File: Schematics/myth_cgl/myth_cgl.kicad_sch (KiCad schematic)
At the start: 9 parts, among them U1002 74LS08, U1003 74LS32, U1013 74AHC04, U1019 74HC02, U1020 74AHC138, U1021 74AHC138, U1022 74AHC244

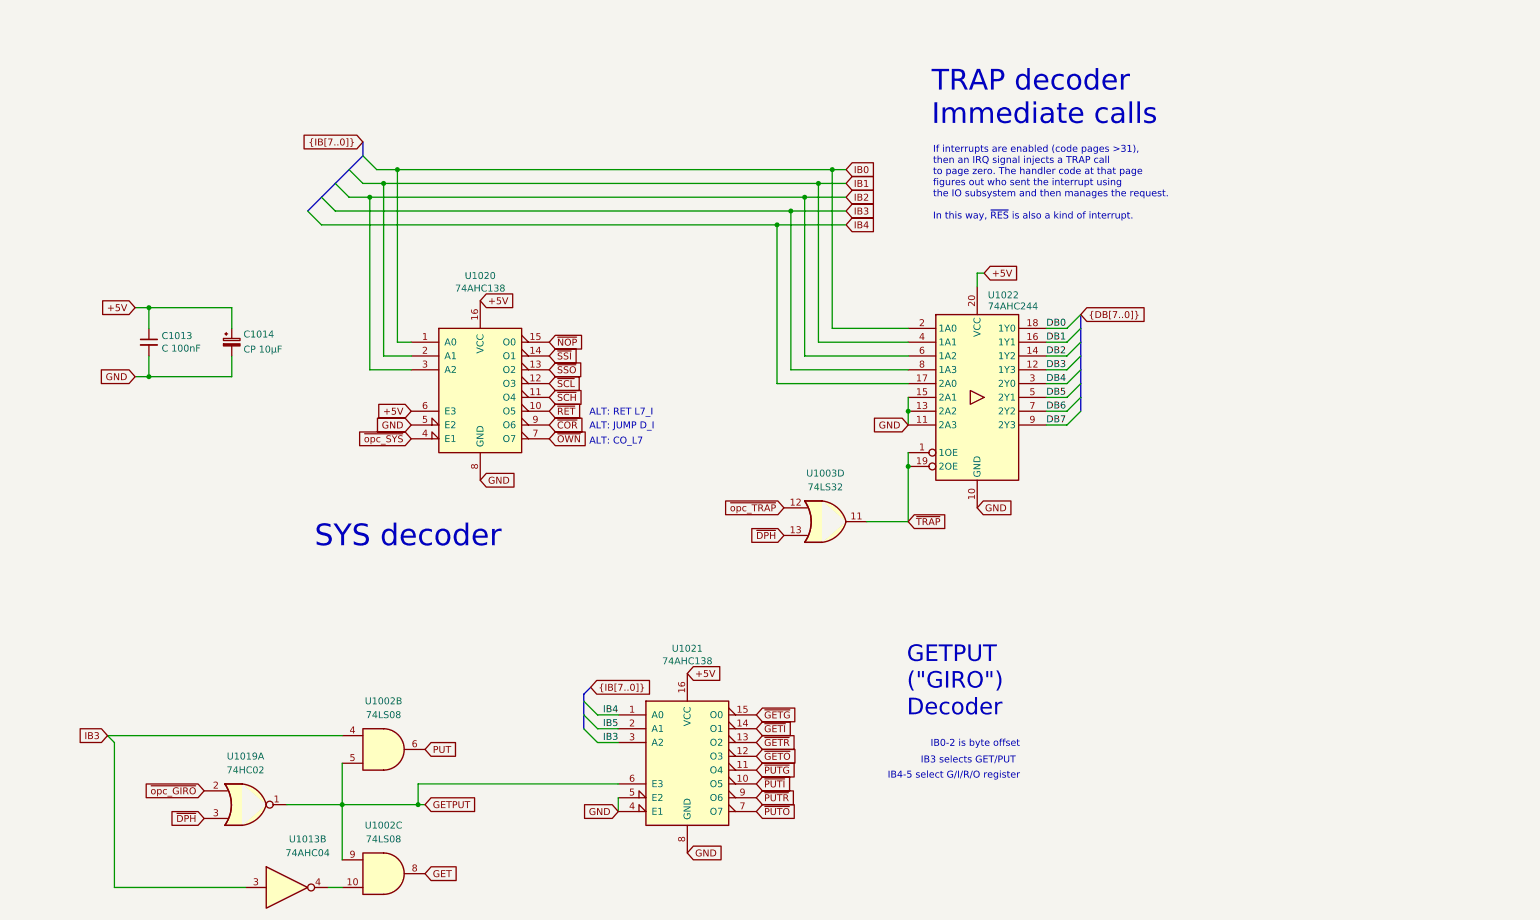
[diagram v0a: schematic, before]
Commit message: Change CO do D
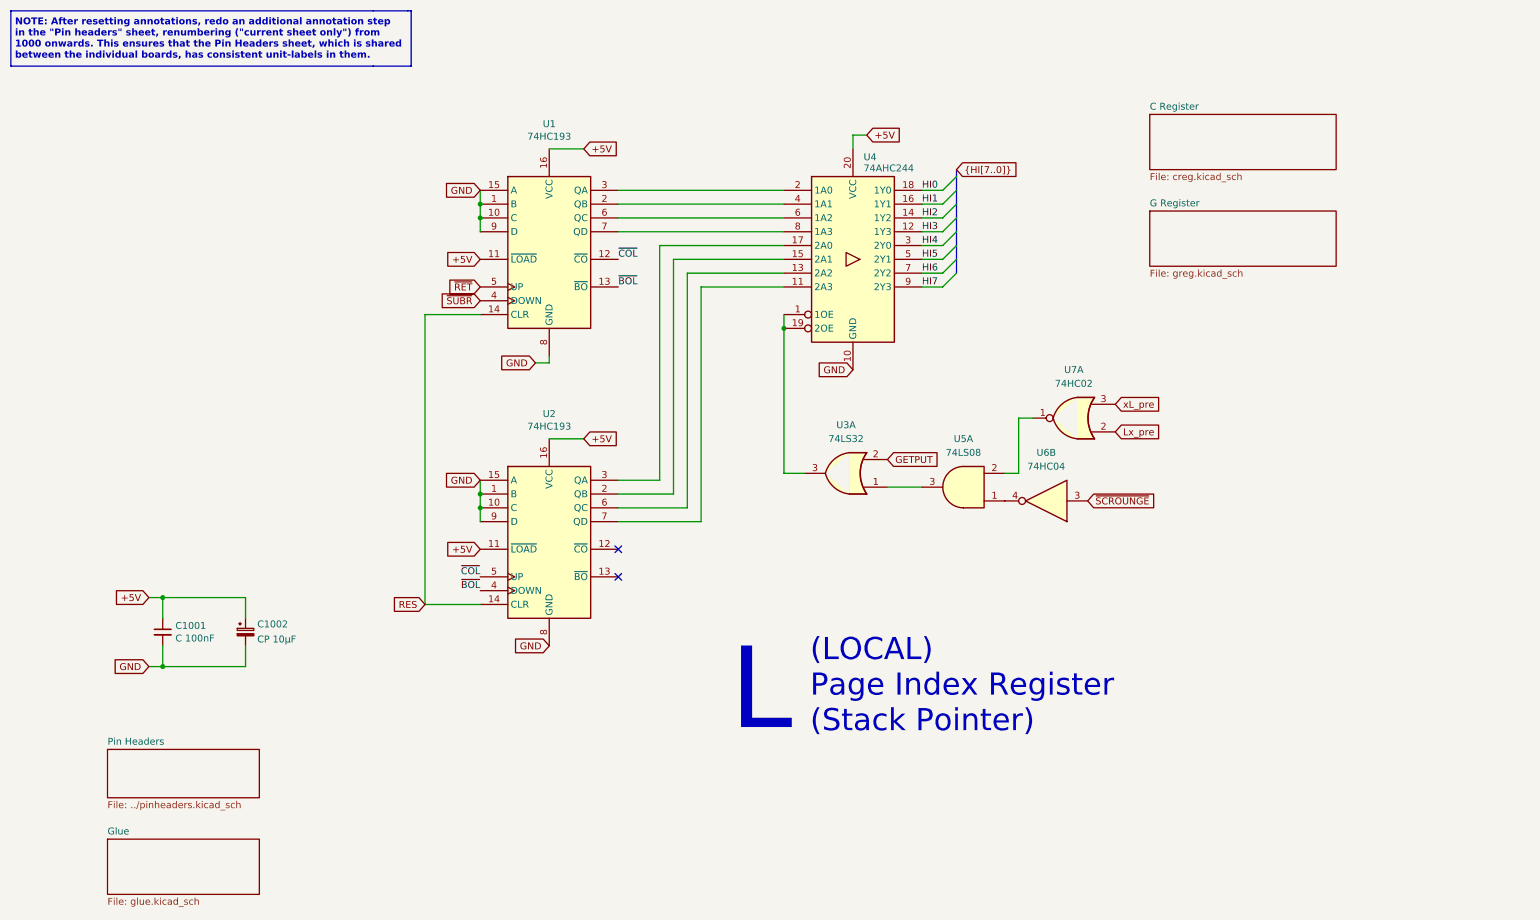
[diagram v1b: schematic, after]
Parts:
- removed C1013: C 100nF, Capacitor_THT:C_Disc_D5.0mm_W2.5mm_P2.50mm, symbol Device:C_Small
- removed C1014: CP 10μF, Capacitor_THT:CP_Radial_D6.3mm_P2.50mm, symbol Device:C_Polarized_Small
- removed U1002: 74LS08, Package_DIP:DIP-14_W7.62mm_Socket_LongPads, symbol 74xx:74LS08
- removed U1003: 74LS32, Package_DIP:DIP-14_W7.62mm_Socket_LongPads, symbol 74xx:74LS32
- removed U1013: 74AHC04, Package_DIP:DIP-14_W7.62mm_Socket_LongPads, symbol 74xx:74AHC04
- removed U1019: 74HC02, Package_DIP:DIP-14_W7.62mm_Socket_LongPads, symbol 74xx:74HC02
- removed U1020, U1021: 74AHC138, Package_DIP:DIP-16_W7.62mm_Socket_LongPads, symbol 74xx:74LS138
- removed U1022: 74AHC244, Package_DIP:DIP-20_W7.62mm_Socket_LongPads, symbol 74xx:74AHC244
- added C1001: C 100nF, Capacitor_THT:C_Disc_D5.0mm_W2.5mm_P2.50mm, symbol Device:C_Small
- added C1002: CP 10μF, Capacitor_THT:CP_Radial_D6.3mm_P2.50mm, symbol Device:C_Polarized_Small
- added U1, U2: 74HC193, Package_DIP:DIP-16_W7.62mm_Socket_LongPads, symbol 74xx:74LS193
- added U3: 74LS32, Package_DIP:DIP-14_W7.62mm_LongPads, symbol 74xx:74LS32
- added U4: 74AHC244, Package_DIP:DIP-20_W7.62mm_Socket_LongPads, symbol 74xx:74AHC244
- added U5: 74LS08, Package_DIP:DIP-14_W7.62mm_LongPads, symbol 74xx:74LS08
- added U6: 74HC04, Package_DIP:DIP-14_W7.62mm_LongPads, symbol 74xx:74HC04
- added U7: 74HC02, Package_DIP:DIP-14_W7.62mm_LongPads, symbol 74xx:74HC02
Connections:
- net +5V: now also C1001.1, C1002.1, U1.11 (~{LOAD}), U1.16 (VCC), U2.11 (~{LOAD}), U2.16 (VCC), U4.20 (VCC)
- net GETPUT: now also U3.2
- net GND: now also C1001.2, C1002.2, U1.1 (B), U1.10 (C), U1.15 (A), U1.8 (GND), U1.9 (D), U2.1 (B), U2.10 (C), U2.15 (A), U2.8 (GND), U2.9 (D), U4.10 (GND)
- net ~{RET}: now also U1.5 (UP)
- new net: U5.1, U6.4
- new net: U5.2, U7.1
- new net: U3.1, U5.3
- new net: U3.3, U4.1 (1OE), U4.19 (2OE)
- new net: U2.7 (QD), U4.11 (2A3)
- new net: U2.6 (QC), U4.13 (2A2)
- new net: U2.2 (QB), U4.15 (2A1)
- new net: U2.3 (QA), U4.17 (2A0)
- new net: U1.3 (QA), U4.2 (1A0)
- new net: U1.2 (QB), U4.4 (1A1)
- new net: U1.6 (QC), U4.6 (1A2)
- new net: U1.7 (QD), U4.8 (1A3)
- new net HI0: U4.18 (1Y0)
- new net HI1: U4.16 (1Y1)
- new net HI2: U4.14 (1Y2)
- new net HI3: U4.12 (1Y3)
- new net HI4: U4.3 (2Y0)
- new net HI5: U4.5 (2Y1)
- new net HI6: U4.7 (2Y2)
- new net HI7: U4.9 (2Y3)
- new net Lx_pre: U7.2
- new net RES: U1.14 (CLR), U2.14 (CLR)
- new net xL_pre: U7.3
- new net ~{BOL}: U1.13 (~{BO}), U2.4 (DOWN)
- new net ~{COL}: U1.12 (~{CO}), U2.5 (UP)
- new net ~{SCROUNGE}: U6.3
- new net ~{SUBR}: U1.4 (DOWN)
- no-connect marks 0 -> 2
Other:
- added sheet C Register (creg.kicad_sch)
- added sheet G Register (greg.kicad_sch)
- added sheet Glue (glue.kicad_sch)
- added sheet Pin Headers (../pinheaders.kicad_sch)
- note added: "(LOCAL) Page Index Register (Stack Pointer)"
- note added: "L"
- note added: "NOTE: After resetting annotations, redo an additional annotation step in the "Pin headers" sheet, renumbering ("current sheet only") from 1000 onwards. This ensures that the Pin Headers sheet, which is shared between the individual boards, has consistent unit-labels in them."
- note removed: "ALT: CO_L7"
- note removed: "ALT: JUMP D_I"
- note removed: "ALT: RET L7_I"
- note removed: "GETPUT ("GIRO") Decoder"
- note removed: "IB0-2 is byte offset"
- note removed: "IB3 selects GET/PUT"
- note removed: "IB4-5 select G/I/R/O register"
- note removed: "If interrupts are enabled (code pages >31), then an IRQ signal injects a TRAP call to page zero. The handler code at that page figures out who sent the interrupt using the IO subsystem and then manages the request. In this way, ~{RES} is also a kind of interrupt."
- note removed: "SYS decoder"
- note removed: "TRAP decoder Immediate calls"

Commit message: Change semantics of xB
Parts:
- added U1006: 74AHC273, Package_DIP:DIP-20_W7.62mm_Socket_LongPads, symbol 74xx:74HC273
- added U1007, U1008: 74HC283, Package_DIP:DIP-16_W7.62mm_Socket_LongPads, symbol 74xx:74LS283
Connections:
- net +5V: now also U1006.20 (VCC), U1007.16 (VCC), U1008.16 (VCC); no longer U1.11 (~{LOAD}), U2.11 (~{LOAD})
- net GND: now also U1006.10 (GND), U1007.7 (C0), U1007.8 (GND), U1008.8 (GND); no longer U1.1 (B), U1.10 (C), U1.15 (A), U1.9 (D), U2.1 (B), U2.10 (C), U2.15 (A), U2.9 (D)
- net at U2.7 (QD), U4.11 (2A3): now also U1006.18 (D7)
- net at U2.6 (QC), U4.13 (2A2): now also U1006.17 (D6)
- net at U2.2 (QB), U4.15 (2A1): now also U1006.14 (D5)
- net at U2.3 (QA), U4.17 (2A0): now also U1006.13 (D4)
- net at U1.3 (QA), U4.2 (1A0): now also U1006.3 (D0)
- net at U1.2 (QB), U4.4 (1A1): now also U1006.4 (D1)
- net at U1.6 (QC), U4.6 (1A2): now also U1006.7 (D2)
- net at U1.7 (QD), U4.8 (1A3): now also U1006.8 (D3)
- new net: U1008.1 (S2), U2.1 (B)
- new net: U1008.13 (S3), U2.10 (C)
- new net: U1008.4 (S1), U2.15 (A)
- new net: U1008.10 (S4), U2.9 (D)
- new net: U1007.9 (C4), U1008.7 (C0)
- new net: U1.1 (B), U1007.1 (S2)
- new net: U1.10 (C), U1007.13 (S3)
- new net: U1.15 (A), U1007.4 (S1)
- new net: U1.9 (D), U1007.10 (S4)
- new net CLOSE: U1006.11 (Cp)
- new net DB0: U1007.5 (A1)
- new net DB1: U1007.3 (A2)
- new net DB2: U1007.14 (A3)
- new net DB3: U1007.12 (A4)
- new net DB4: U1008.5 (A1)
- new net DB5: U1008.3 (A2)
- new net DB6: U1008.14 (A3)
- new net DB7: U1008.12 (A4)
- new net L0: U1006.2 (Q0), U1007.6 (B1)
- new net L1: U1006.5 (Q1), U1007.2 (B2)
- new net L2: U1006.6 (Q2), U1007.15 (B3)
- new net L3: U1006.9 (Q3), U1007.11 (B4)
- new net L4: U1006.12 (Q4), U1008.6 (B1)
- new net L5: U1006.15 (Q5), U1008.2 (B2)
- new net L6: U1006.16 (Q6), U1008.15 (B3)
- new net L7: U1006.19 (Q7), U1008.11 (B4)
- new net ~{RES}: U1006.1 (~{Mr})
- new net ~{xLFIX}: U1.11 (~{LOAD}), U2.11 (~{LOAD})
- no-connect marks 2 -> 3
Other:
- note added: "ADDER"
- moved on the sheet: C1001, C1002, U1, U2, U3A, U4, U5A, U6B, U7A

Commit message: Let defines/labels diverge from assembler mnemonics
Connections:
- net ~{xLFIX} renamed ~{xNEAR}
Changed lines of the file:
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@@
 		)
 	)
-	(label "~{xLFIX}"
+	(label "~{xNEAR}"
 		(at 83.82 104.14 180)
 		(fields_autoplaced yes)
